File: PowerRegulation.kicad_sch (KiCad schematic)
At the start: 37 parts, among them J10 XT60-M, J11 24V_Lockout_Key_Switch, K1 G5Q-1A DC24, Q7 BSS138, U6 TPS5430DDA, U7 XC6220B331PR-G

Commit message: minor fixed + lowered status leds to ~0.6mA, which should give ~50 mcd
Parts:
- R29, R32, R33: value 22k -> 39k
- R40: value 1k -> 3.3k
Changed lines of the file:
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@@
 		(fields_autoplaced yes)
 		(property "Reference" "R40"
-			(at 264.16 73.6601 0)
+			(at 259.08 71.1199 0)
 			(effects
 				(font
 					(size 1.27 1.27)
 				)
-				(justify left)
+				(justify right)
 			)
 		)
-		(property "Value" "1k"
-			(at 264.16 71.1201 0)
+		(property "Value" "3.3k"
+			(at 259.08 73.6599 0)
 			(effects
 				(font
 					(size 1.27 1.27)
 				)
-				(justify left)
+				(justify right)
 			)
 		)
@@
 		(fields_autoplaced yes)
 		(property "Reference" "R29"
-			(at 39.37 135.8901 0)
+			(at 34.29 133.3499 0)
 			(effects
 				(font
 					(size 1.27 1.27)
 				)
-				(justify left)
+				(justify right)
 			)
 		)
-		(property "Value" "22k"
-			(at 39.37 133.3501 0)
+		(property "Value" "39k"
+			(at 34.29 135.8899 0)
 			(effects
 				(font
 					(size 1.27 1.27)
 				)
-				(justify left)
+				(justify right)
 			)
 		)
@@
 		(fields_autoplaced yes)
 		(property "Reference" "R32"
-			(at 71.12 78.7401 0)
+			(at 66.04 76.1999 0)
 			(effects
 				(font
 					(size 1.27 1.27)
 				)
-				(justify left)
+				(justify right)
 			)
 		)
-		(property "Value" "22k"
-			(at 71.12 76.2001 0)
+		(property "Value" "39k"
+			(at 66.04 78.7399 0)
 			(effects
 				(font
 					(size 1.27 1.27)
 				)
-				(justify left)
+				(justify right)
 			)
 		)
@@
 		(fields_autoplaced yes)
 		(property "Reference" "R33"
-			(at 82.55 148.5901 0)
+			(at 77.47 146.0499 0)
 			(effects
 				(font
 					(size 1.27 1.27)
 				)
-				(justify left)
+				(justify right)
 			)
 		)
-		(property "Value" "22k"
-			(at 82.55 146.0501 0)
+		(property "Value" "39k"
+			(at 77.47 148.5899 0)
 			(effects
 				(font
 					(size 1.27 1.27)
 				)
-				(justify left)
+				(justify right)
 			)
 		)

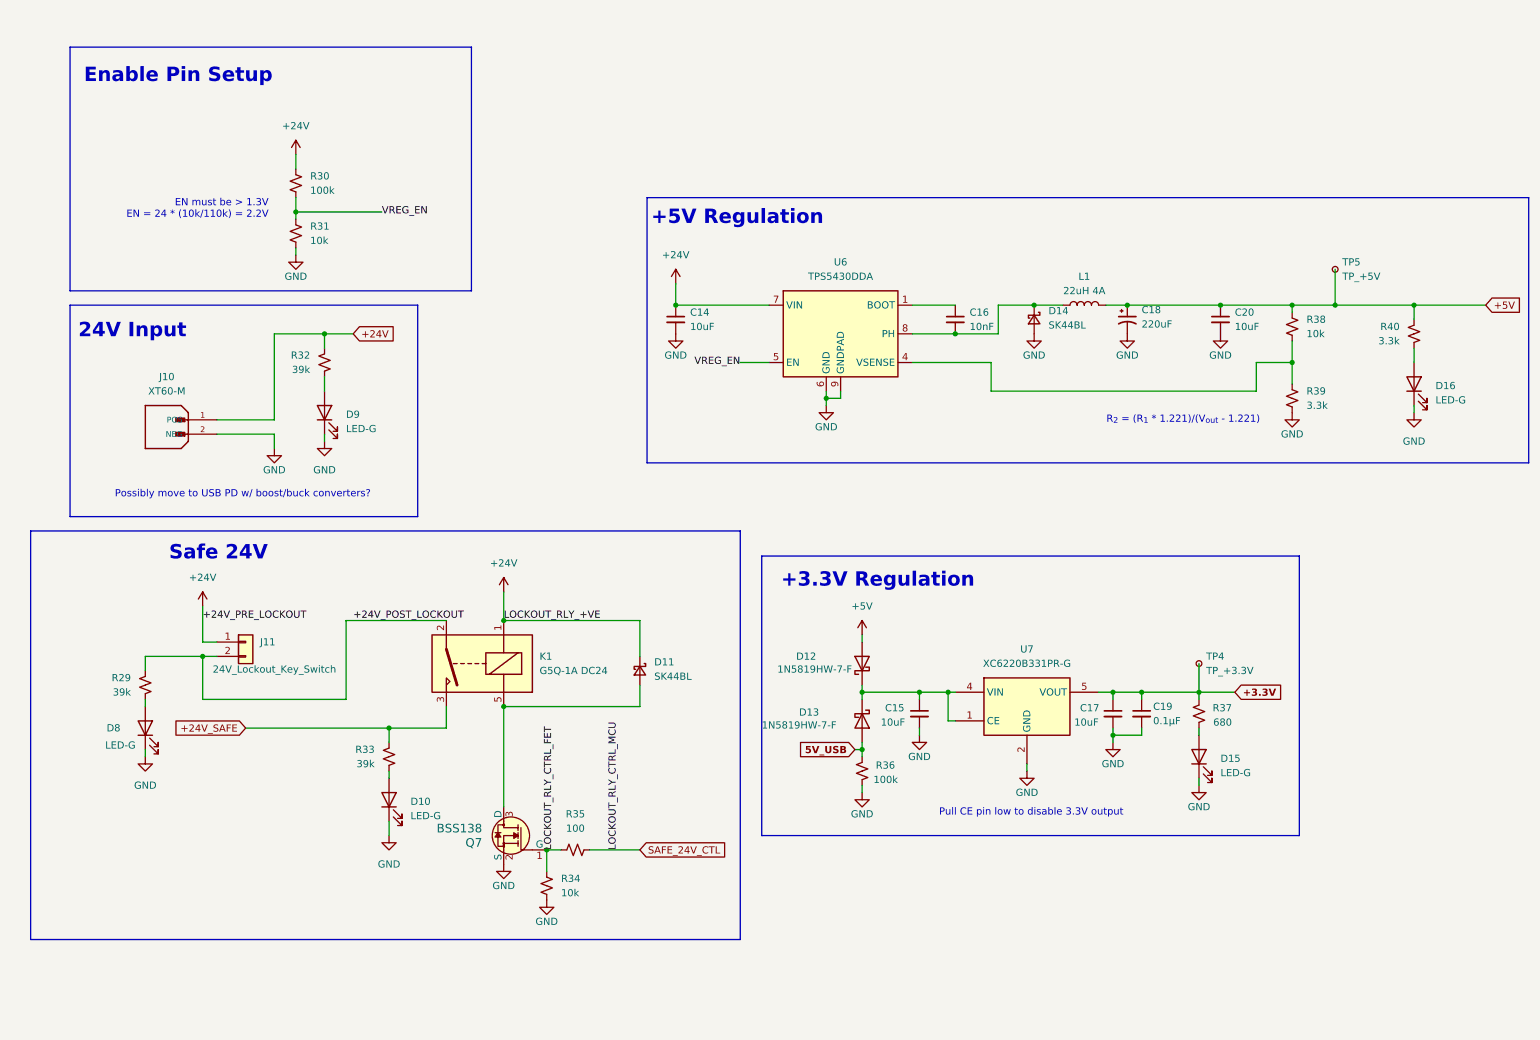
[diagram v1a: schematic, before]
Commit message: revamped schematic to be more readable
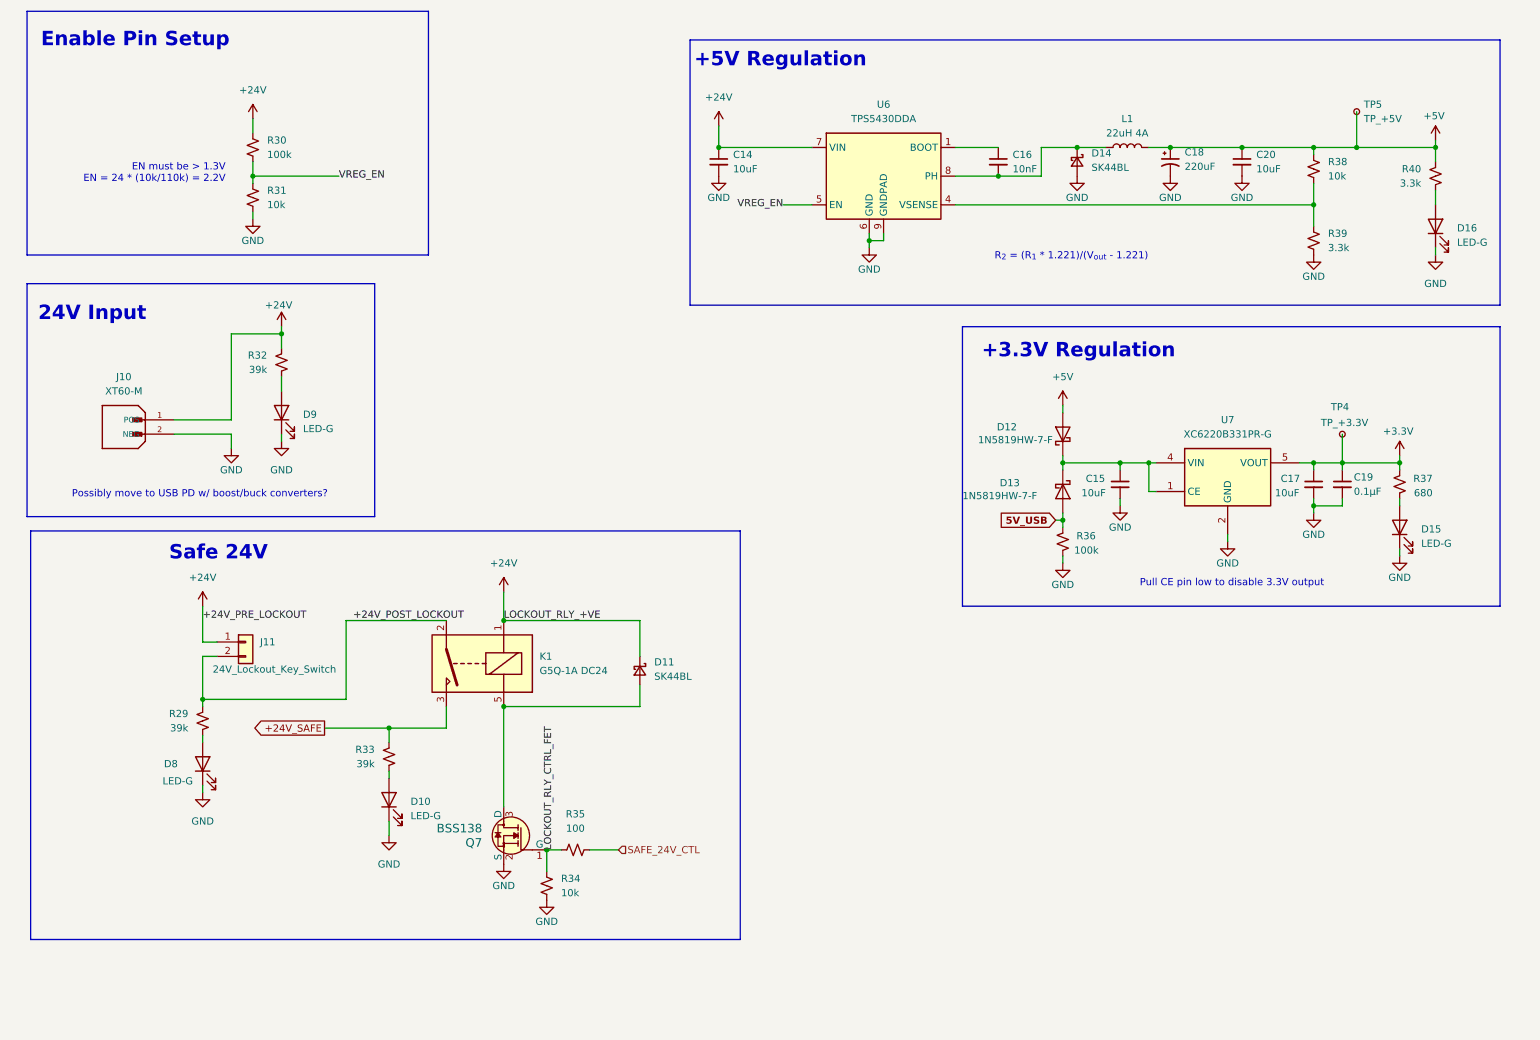
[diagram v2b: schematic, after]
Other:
- moved on the sheet: C14, C15, C16, C17, C18, C19, C20, D12, D13, D14, D15, D16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

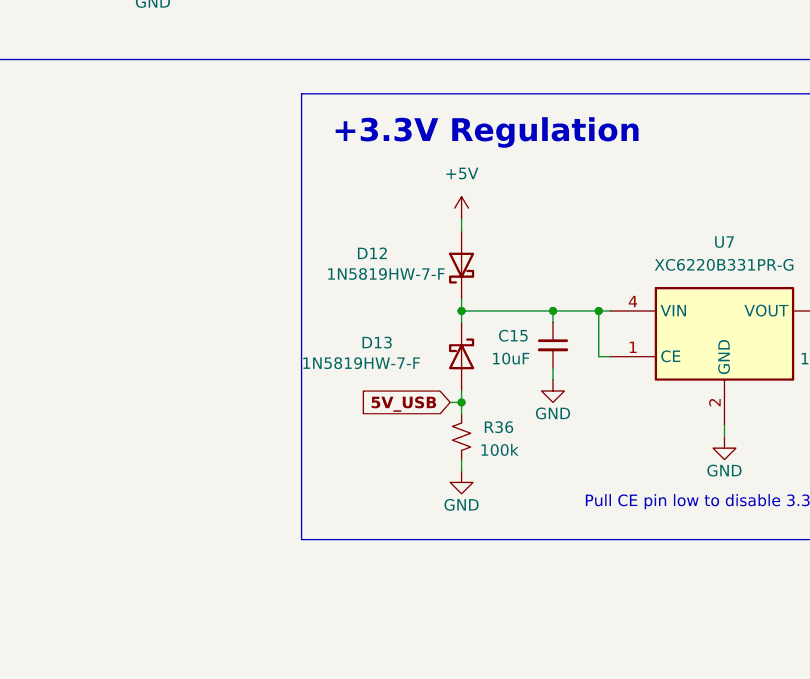
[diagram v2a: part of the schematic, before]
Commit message: remove diode between 5V and 5V_USB due to oversight (ADS112C04 cannot have DVDD without AVDD)
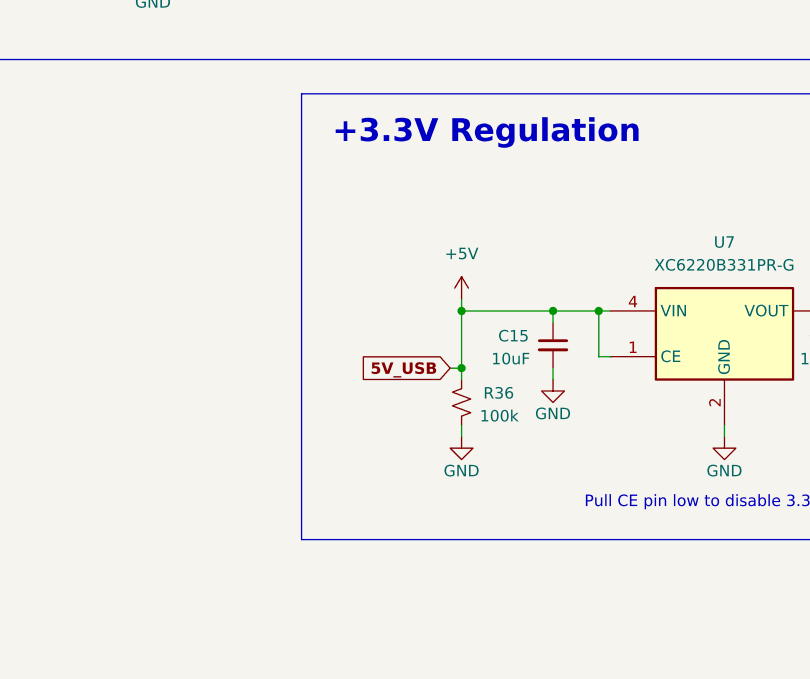
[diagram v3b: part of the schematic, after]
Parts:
- removed D12, D13: 1N5819HW-7-F, Diode_SMD:D_SOD-123, symbol Diode:MBR0540
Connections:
- net 5V_USB is gone; now on net +5V: R36.2
- net +5V: now also C15.1, U7.1 (CE), U7.4 (NC)
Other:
- moved on the sheet: R36
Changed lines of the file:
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@@
 	)
 	(junction
-		(at 199.39 105.41)
+		(at 199.39 101.6)
 		(diameter 0)
 		(color 0 0 0 0)
@@
 	(wire
 		(pts
-			(xy 199.39 111.76) (xy 199.39 113.03)
+			(xy 199.39 107.95) (xy 199.39 109.22)
 		)
 		(stroke
@@
 	(wire
 		(pts
-			(xy 199.39 105.41) (xy 199.39 106.68)
+			(xy 199.39 101.6) (xy 199.39 102.87)
 		)
 		(stroke
@@
 	(wire
 		(pts
-			(xy 199.39 95.25) (xy 199.39 96.52)
-		)
-		(stroke
-			(width 0)
-			(type default)
-		)
-	)
-	(wire
-		(pts
 			(xy 72.39 123.19) (xy 72.39 137.16)
 		)
@@
 	(wire
 		(pts
-			(xy 198.12 105.41) (xy 199.39 105.41)
+			(xy 198.12 101.6) (xy 199.39 101.6)
+		)
+		(stroke
+			(width 0)
+			(type default)
+		)
+	)
+	(wire
+		(pts
+			(xy 199.39 95.25) (xy 199.39 101.6)
 		)
 		(stroke
@@
 	(wire
 		(pts
-			(xy 199.39 85.09) (xy 199.39 86.36)
-		)
-		(stroke
-			(width 0)
-			(type default)
-		)
-	)
-	(wire
-		(pts
 			(xy 55.88 44.45) (xy 71.12 44.45)
 		)
@@
 	(wire
 		(pts
-			(xy 199.39 105.41) (xy 199.39 104.14)
-		)
-		(stroke
-			(width 0)
-			(type default)
-		)
-	)
-	(wire
-		(pts
 			(xy 265.43 38.1) (xy 265.43 39.37)
 		)
@@
 	(global_label "5V_USB"
 		(shape input)
-		(at 198.12 105.41 180)
+		(at 198.12 101.6 180)
 		(fields_autoplaced yes)
 		(effects
@@
 		)
 		(property "Intersheetrefs" "${INTERSHEET_REFS}"
-			(at 187.5831 105.41 0)
+			(at 187.5831 101.6 0)
 			(effects
 				(font
@@
 	)
 	(symbol
-		(lib_id "Diode:MBR0540")
-		(at 199.39 100.33 270)
-		(unit 1)
-		(exclude_from_sim no)
-		(in_bom yes)
-		(on_board yes)
-		(dnp no)
-		(property "Reference" "D13"
-			(at 188.214 98.806 90)
-			(effects
-				(font
-					(size 1.27 1.27)
-				)
-				(justify left)
-			)
-		)
-		(property "Value" "1N5819HW-7-F"
-			(at 181.61 101.092 90)
-			(effects
-				(font
-					(size 1.27 1.27)
-				)
-				(justify left)
-			)
-		)
-		(property "Footprint" "Diode_SMD:D_SOD-123"
-			(at 194.945 100.33 0)
-			(effects
-				(font
-					(size 1.27 1.27)
-				)
-				(hide yes)
-			)
-		)
-		(property "Datasheet" "http://www.mccsemi.com/up_pdf/MBR0520~MBR0580(SOD123).pdf"
-			(at 199.39 100.33 0)
-			(effects
-				(font
-					(size 1.27 1.27)
-				)
-				(hide yes)
-			)
-		)
-		(property "Description" "40V 0.5A Schottky Power Rectifier Diode, SOD-123"
-			(at 199.39 100.33 0)
-			(effects
-				(font
-					(size 1.27 1.27)
-				)
-				(hide yes)
-			)
-		)
-		(pin "2"
-		)
-		(pin "1"
-		)
-		(instances
-			(project "panda"
-				(path "/226c5870-4123-4efa-a2b3-b42d02f59bb7/9fa93f08-739d-4753-8e9a-eafbcf15bffc"
-					(reference "D13")
-					(unit 1)
-				)
-			)
-			(project ""
-				(path "/936199fd-7e49-4734-a2ef-dd7d42ccdc61"
-					(reference "D5")
-					(unit 1)
-				)
-			)
-		)
-	)
-	(symbol
 		(lib_id "Device:R_Small_US")
 		(at 259.08 99.06 0)
@@
 	(symbol
 		(lib_id "power:GND")
-		(at 199.39 113.03 0)
+		(at 199.39 109.22 0)
 		(unit 1)
 		(exclude_from_sim no)
@@
 		(dnp no)
 		(property "Reference" "#PWR089"
-			(at 199.39 119.38 0)
+			(at 199.39 115.57 0)
 			(effects
 				(font
@@
 		)
 		(property "Value" "GND"
-			(at 199.39 116.84 0)
+			(at 199.39 113.03 0)
 			(effects
 				(font
@@
 		)
 		(property "Footprint" ""
-			(at 199.39 113.03 0)
+			(at 199.39 109.22 0)
 			(effects
 				(font
@@
 		)
 		(property "Datasheet" ""
-			(at 199.39 113.03 0)
+			(at 199.39 109.22 0)
 			(effects
 				(font
@@
 		)
 		(property "Description" "Power symbol creates a global label with name \"GND\" , ground"
-			(at 199.39 113.03 0)
+			(at 199.39 109.22 0)
 			(effects
 				(font
@@
 	(symbol
 		(lib_id "Device:R_Small_US")
-		(at 199.39 109.22 0)
+		(at 199.39 105.41 0)
 		(mirror x)
 		(unit 1)
@@
 		(dnp no)
 		(property "Reference" "R36"
-			(at 205.232 108.204 0)
+			(at 205.232 104.394 0)
 			(effects
 				(font
@@
 		)
 		(property "Value" "100k"
-			(at 205.74 110.744 0)
+			(at 205.74 106.934 0)
 			(effects
 				(font
@@
 		)
 		(property "Footprint" "Resistor_SMD:R_0402_1005Metric"
-			(at 199.39 109.22 0)
+			(at 199.39 105.41 0)
 			(effects
 				(font
@@
 		)
 		(property "Datasheet" "~"
-			(at 199.39 109.22 0)
+			(at 199.39 105.41 0)
 			(effects
 				(font
@@
 		)
 		(property "Description" "Resistor, small US symbol"
-			(at 199.39 109.22 0)
+			(at 199.39 105.41 0)
 			(effects
 				(font
@@
 	)
 	(symbol
-		(lib_id "Diode:MBR0540")
-		(at 199.39 90.17 90)
-		(unit 1)
-		(exclude_from_sim no)
-		(in_bom yes)
-		(on_board yes)
-		(dnp no)
-		(property "Reference" "D12"
-			(at 191.262 88.9 90)
-			(effects
-				(font
-					(size 1.27 1.27)
-				)
-				(justify left)
-			)
-		)
-		(property "Value" "1N5819HW-7-F"
-			(at 197.612 91.186 90)
-			(effects
-				(font
-					(size 1.27 1.27)
-				)
-				(justify left)
-			)
-		)
-		(property "Footprint" "Diode_SMD:D_SOD-123"
-			(at 203.835 90.17 0)
-			(effects
-				(font
-					(size 1.27 1.27)
-				)
-				(hide yes)
-			)
-		)
-		(property "Datasheet" "http://www.mccsemi.com/up_pdf/MBR0520~MBR0580(SOD123).pdf"
-			(at 199.39 90.17 0)
-			(effects
-				(font
-					(size 1.27 1.27)
-				)
-				(hide yes)
-			)
-		)
-		(property "Description" "40V 0.5A Schottky Power Rectifier Diode, SOD-123"
-			(at 199.39 90.17 0)
-			(effects
-				(font
-					(size 1.27 1.27)
-				)
-				(hide yes)
-			)
-		)
-		(pin "2"
-		)
-		(pin "1"
-		)
-		(instances
-			(project "panda"
-				(path "/226c5870-4123-4efa-a2b3-b42d02f59bb7/9fa93f08-739d-4753-8e9a-eafbcf15bffc"
-					(reference "D12")
-					(unit 1)
-				)
-			)
-			(project "PowerRegulation"
-				(path "/936199fd-7e49-4734-a2ef-dd7d42ccdc61"
-					(reference "D4")
-					(unit 1)
-				)
-			)
-		)
-	)
-	(symbol
 		(lib_id "power:+5V")
-		(at 199.39 85.09 0)
+		(at 199.39 93.98 0)
 		(unit 1)
 		(exclude_from_sim no)
@@
 		(dnp no)
 		(property "Reference" "#PWR088"
-			(at 199.39 88.9 0)
+			(at 199.39 97.79 0)
 			(effects
 				(font
@@
 		)
 		(property "Value" "+5V"
-			(at 199.39 80.01 0)
+			(at 199.39 88.9 0)
 			(effects
 				(font
@@
 		)
 		(property "Footprint" ""
-			(at 199.39 85.09 0)
+			(at 199.39 93.98 0)
 			(effects
 				(font
@@
 		)
 		(property "Datasheet" ""
-			(at 199.39 85.09 0)
+			(at 199.39 93.98 0)
 			(effects
 				(font
@@
 		)
 		(property "Description" "Power symbol creates a global label with name \"+5V\""
-			(at 199.39 85.09 0)
+			(at 199.39 93.98 0)
 			(effects
 				(font
